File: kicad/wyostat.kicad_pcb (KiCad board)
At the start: 2 copper layers, 99.1 x 99.1 mm, 98 parts, among them J1 24 V AC IN, J10 Y2, J11 G, J12 W1, J13 USB_microAB, J14 W2, J16 5V_SEL, J2 OUT1, J3 OUT2, J4 OUT3, J5 I2C_ext1, J6 RH, J7 RC, J8 C, J9 Y1, Q1 BTA204S, Q2 BTA204S, Q3 BTA204S, U1 MOC3063M, U2 MOC3063M, U3 MOC3063M, U4 Wemos-Lolin, U5 MAX17502FATB+T, U6 DS3231N

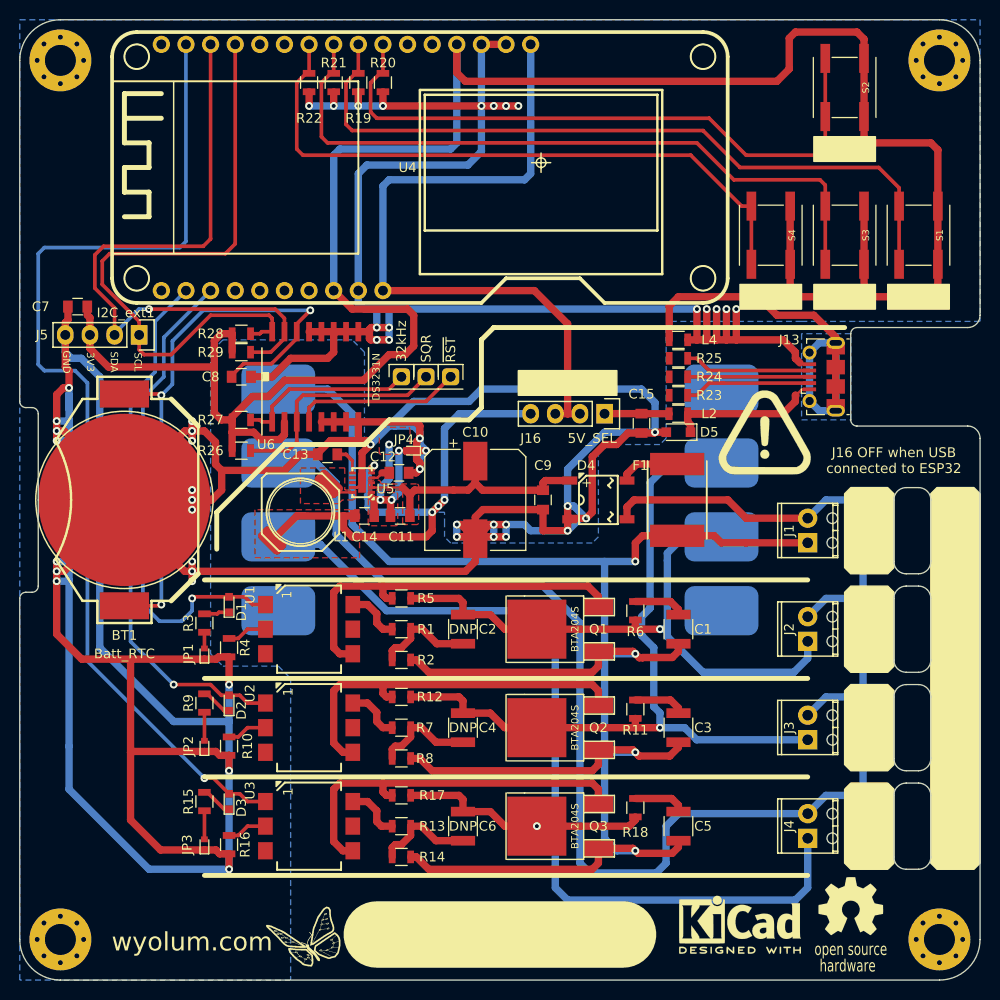
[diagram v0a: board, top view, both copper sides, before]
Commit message: footprint corrections on PCB
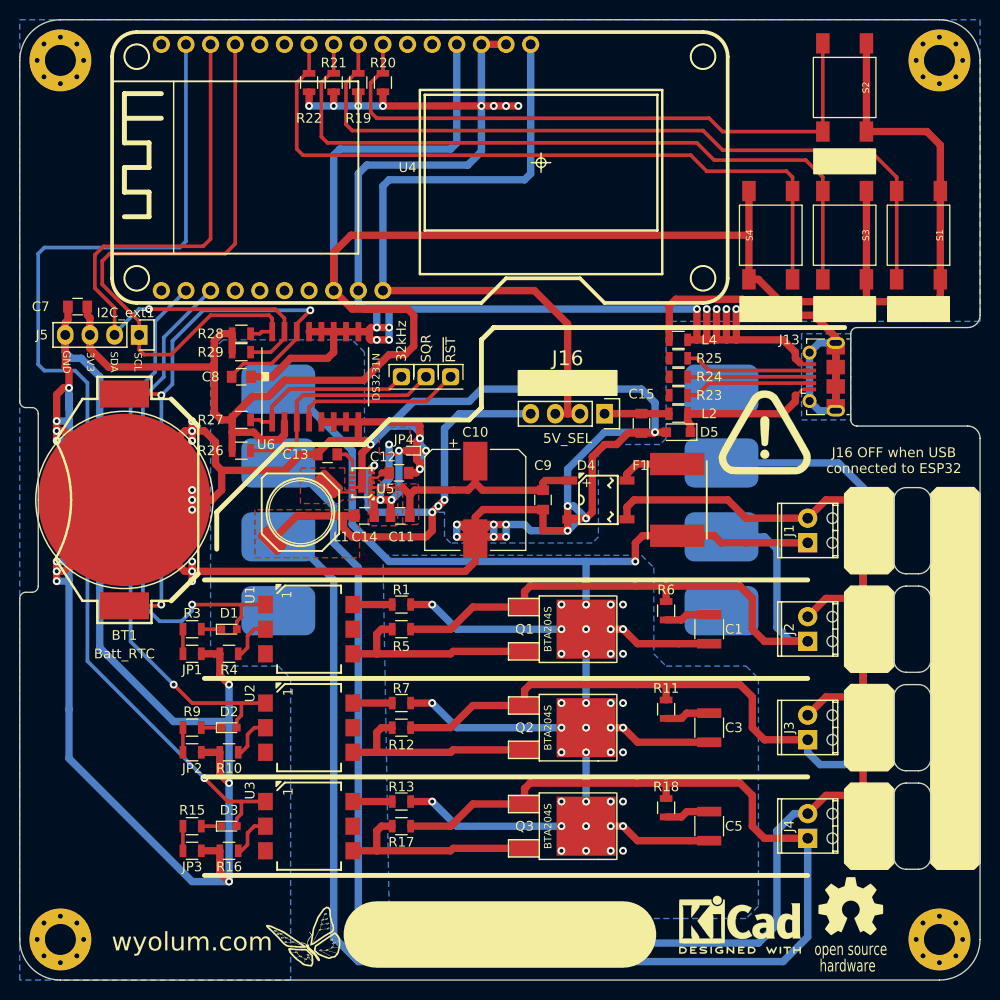
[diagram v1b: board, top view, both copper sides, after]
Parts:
- removed C2, C4, C6: 47nF,63V, wyostat_fp:C_1210
- removed R14, R2, R8: 0E, wyostat_fp:R_0805
- D5: footprint Diodes_SMD:D_SOD-323_HandSoldering -> wyostat_fp:D_SOD-323_HandSoldering
- JP1, JP2, JP3: footprint wyostat_fp:LED_0402 -> wyostat_fp:R_0805
- Logo5: renamed from G***; value LOGO -> logo_warning
- S1, S2, S3, S4: footprint wyostat_fp:SW_SPST_CK_KSCx -> wyostat_fp:SW_SPST_FSM6JSMA
- moved Q1 7.62 mm to (83.8, 94.6), turned to 270 degrees
- moved Q2 7.62 mm to (83.8, 104.8), turned to 270 degrees
- moved Q3 7.62 mm to (83.8, 114.9), turned to 270 degrees
- moved C1 3.18 mm to (102.9, 94.6)
- moved C3 3.18 mm to (102.9, 104.8)
- moved C5 3.18 mm to (102.9, 114.9)
- moved R12 3.18 mm to (71.1, 104.8)
- moved R11 3.17 mm to (98.4, 102.9), turned to 270 degrees
- moved R17 3.17 mm to (71.1, 114.9)
- moved R18 3.17 mm to (98.4, 113.0), turned to 270 degrees
- moved R5 3.17 mm to (71.1, 94.6)
- moved R6 3.17 mm to (98.4, 92.7), turned to 270 degrees
- moved R15 2.84 mm to (49.5, 114.9), turned to 0 degrees
- moved R9 2.84 mm to (49.5, 104.8), turned to 0 degrees
- moved D2 2.54 mm to (53.3, 104.8), turned to 0 degrees
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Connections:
- net /5V_IN1 renamed /5V_EXT
- net /5V_IN2 renamed /5V_USB
- J10 pad 1: /Y2 -> (no net)
- J14 pad 1: /W2 -> (no net)
- J7 pad 1: /Rc -> (no net)
- Q1 pad 1: /24Vac-H -> /OUT1
- Q1 pad 2: /OUT1 -> /24Vac-H
- Q2 pad 1: /24Vac-H -> /OUT2
- Q2 pad 2: /OUT2 -> /24Vac-H
- Q3 pad 1: /24Vac-H -> /OUT3
- Q3 pad 2: /OUT3 -> /24Vac-H
- R1 pad 1: Net-(C2-Pad1) -> /24Vac-H
- R13 pad 1: Net-(C6-Pad1) -> /24Vac-H
- R23 pad 1: /USB_D- -> (no net)
- R24 pad 1: /USB_D+ -> (no net)
- R25 pad 1: /USB_ID -> (no net)
- R7 pad 1: Net-(C4-Pad1) -> /24Vac-H
- U1 pad 3: Net-(U1-Pad3) -> (no net)
- U1 pad 5: Net-(U1-Pad5) -> (no net)
- U2 pad 3: Net-(U2-Pad3) -> (no net)
- U2 pad 5: Net-(U2-Pad5) -> (no net)
- U3 pad 3: Net-(U3-Pad3) -> (no net)
- U3 pad 5: Net-(U3-Pad5) -> (no net)
- U4 pad 1: Net-(U4-Pad1) -> (no net)
- U4 pad 11: Net-(U4-Pad11) -> (no net)
- U4 pad 12: Net-(U4-Pad12) -> (no net)
- U4 pad 20: Net-(U4-Pad20) -> (no net)
- U4 pad 21: Net-(U4-Pad21) -> (no net)
- U4 pad 22: Net-(U4-Pad22) -> (no net)
- U4 pad 23: Net-(U4-Pad23) -> (no net)
- U4 pad 26: Net-(U4-Pad26) -> (no net)
- U4 pad 5: Net-(U4-Pad5) -> (no net)
- U4 pad 6: Net-(U4-Pad6) -> (no net)
- U5 pad 7: Net-(U5-Pad7) -> (no net)
- U5 pad 8: /R -> (no net)
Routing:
- net GND: track 671.5 -> 620.7 mm
- net /OUT3: track 120.1 -> 156.1 mm, vias 1 -> 0
- net /OUT2: track 79.1 -> 100.2 mm, vias 1 -> 0
- net Net-(Q3-Pad3): track 39.1 -> 21.7 mm
- net Net-(Q2-Pad3): track 39.1 -> 21.7 mm
- net Net-(Q1-Pad3): track 39.1 -> 21.7 mm
- net /24Vac-C: track 170.8 -> 186.5 mm
- net Net-(C2-Pad1): track 10.4 -> 0.00 mm
- net Net-(C6-Pad1): track 10.4 -> 0.00 mm
- net Net-(C4-Pad1): track 10.4 -> 0.00 mm
- net /24Vac-H: track 203.3 -> 193.7 mm, vias 4 -> 40
- net /SW_M: track 66.8 -> 74.4 mm
- net /3V3: track 229.9 -> 235.9 mm
- net /OUT1: track 62.7 -> 67.6 mm, vias 1 -> 0
- net /IN3: track 106.4 -> 109.2 mm
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- added copper zone on B.Cu, net /24Vac-H

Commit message: PCB updated for 2nd round of prototype
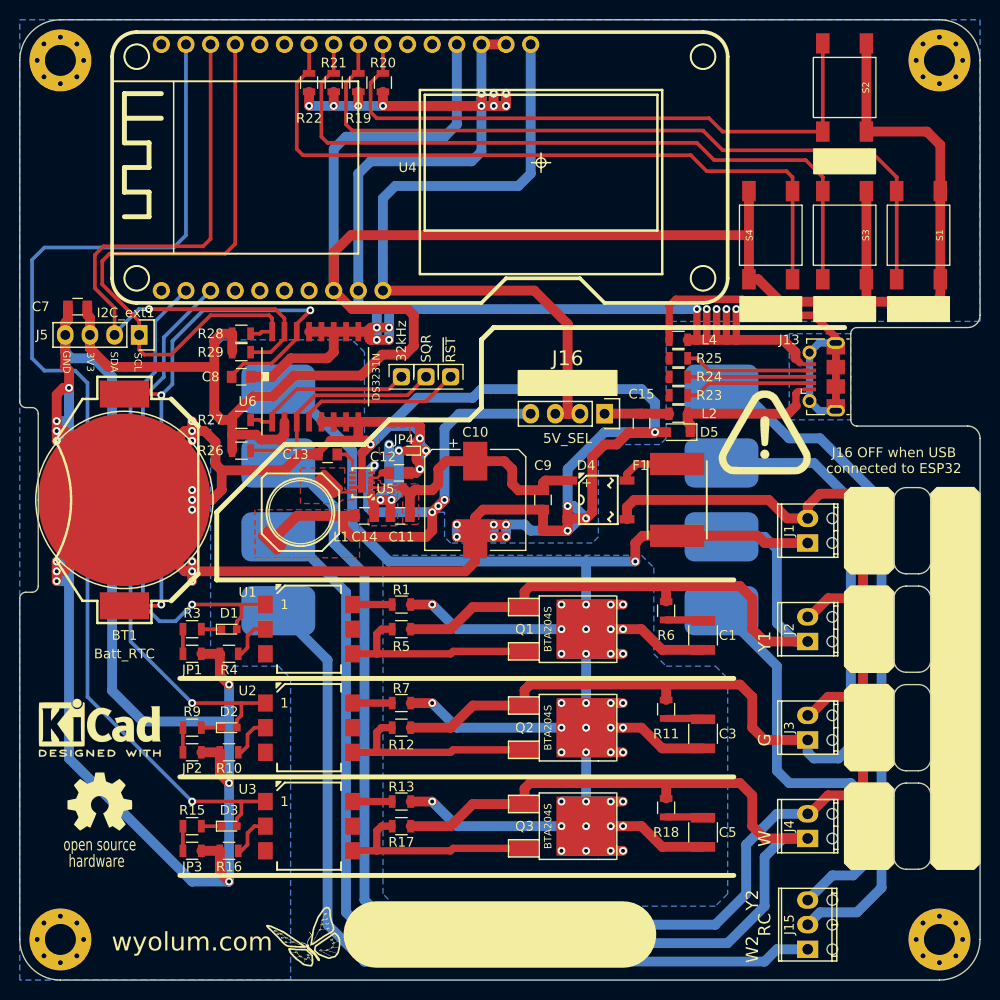
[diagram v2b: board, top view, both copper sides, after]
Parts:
- added J15: Conn_Spare, wyostat_fp:TerminalBlock_Pheonix_MPT-2.54mm_3pol, F.Cu at (113.0, 125.1)
- moved Logo2 78.2 mm to (40.0, 112.4)
- moved Logo3 69.1 mm to (40.0, 104.8)
- moved Logo4 26.7 mm to (81.9, 54.6)
- moved C1 0.90 mm to (102.2, 95.2)
- moved C3 0.90 mm to (102.2, 105.4)
- moved C5 0.90 mm to (102.2, 115.6)
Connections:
- J10 pad 1: (no net) -> /Y2
- J14 pad 1: (no net) -> /W2
- J7 pad 1: (no net) -> /RC
- R23 pad 1: (no net) -> /USB_D-
- R24 pad 1: (no net) -> /USB_D+
- R25 pad 1: (no net) -> /USB_ID
- U1 pad 3: (no net) -> Net-(U1-Pad3)
- U1 pad 5: (no net) -> Net-(U1-Pad5)
- U2 pad 3: (no net) -> Net-(U2-Pad3)
- U2 pad 5: (no net) -> Net-(U2-Pad5)
- U3 pad 3: (no net) -> Net-(U3-Pad3)
- U3 pad 5: (no net) -> Net-(U3-Pad5)
- U4 pad 1: (no net) -> Net-(U4-Pad1)
- U4 pad 11: (no net) -> Net-(U4-Pad11)
- U4 pad 12: (no net) -> Net-(U4-Pad12)
- U4 pad 20: (no net) -> Net-(U4-Pad20)
- U4 pad 21: (no net) -> Net-(U4-Pad21)
- U4 pad 22: (no net) -> Net-(U4-Pad22)
- U4 pad 23: (no net) -> Net-(U4-Pad23)
- U4 pad 26: (no net) -> Net-(U4-Pad26)
- U4 pad 5: (no net) -> Net-(U4-Pad5)
- U4 pad 6: (no net) -> Net-(U4-Pad6)
- U5 pad 7: (no net) -> Net-(U5-Pad7)
- U5 pad 8: (no net) -> /R
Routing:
- net /24Vac-H: track 193.7 -> 284.0 mm
- net /W2: track 0.00 -> 86.1 mm
- net /RC: track 0.00 -> 70.4 mm
- net /Y2: track 0.00 -> 43.2 mm
- net /OUT3: track 156.1 -> 148.3 mm
- net GND: track 620.7 -> 627.1 mm, vias 54 -> 56
- net /24Vac-C: track 186.5 -> 181.7 mm
- net /OUT2: track 100.2 -> 96.4 mm
- net /IN3: track 109.2 -> 111.5 mm
- net /40VDC: track 27.4 -> 28.8 mm
- net /USB+: track 17.5 -> 16.4 mm
- net /3V3: track 235.9 -> 235.1 mm
- net Net-(C5-Pad2): track 4.67 -> 3.85 mm
- net Net-(C1-Pad2): track 4.67 -> 3.85 mm
- net Net-(C3-Pad2): track 4.67 -> 3.85 mm
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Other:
- board text added: "W"
- board text added: "W2"

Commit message: added Sparkfun TMP102 footprint and PCB edges modified
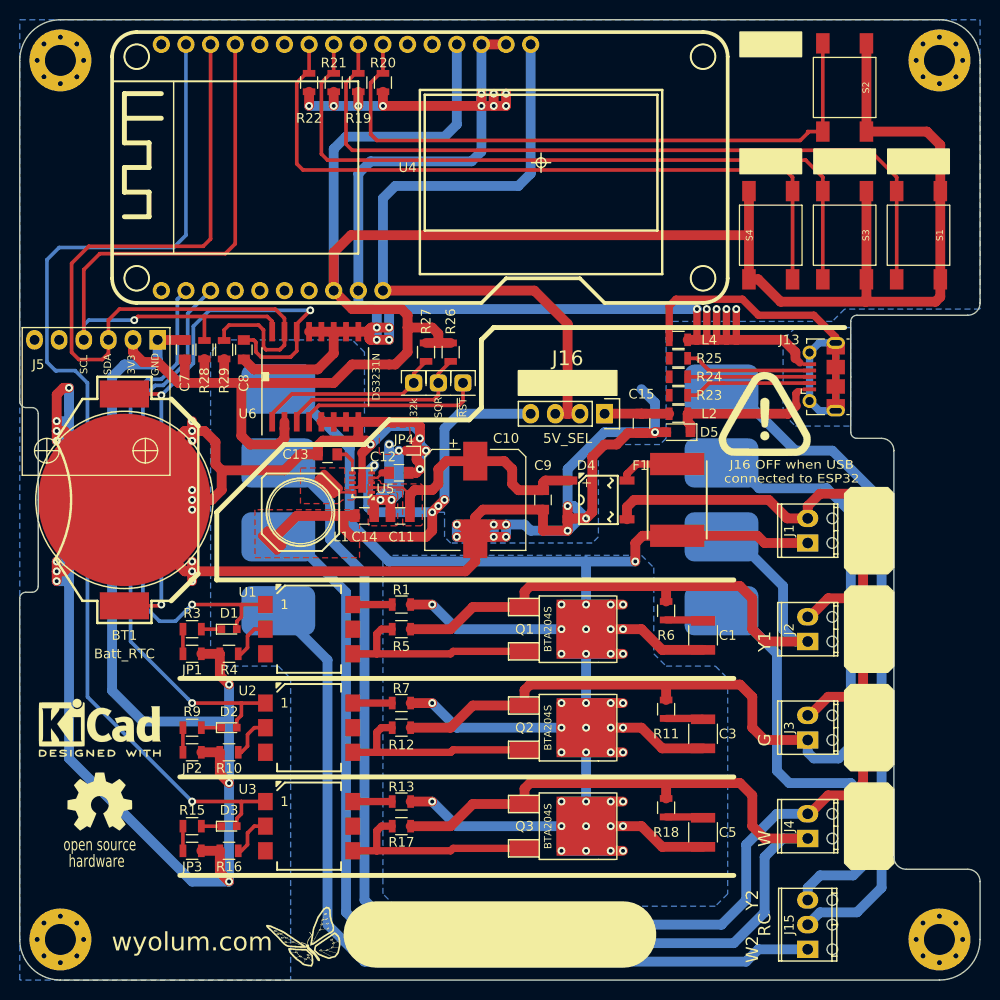
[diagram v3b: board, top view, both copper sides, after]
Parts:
- J5: footprint wyostat_fp:Pin_Header_Straight_1x04 -> wyostat_fp:Pin_Header_TMP102_1x06
- TP3: value 32kHz -> 32k
- moved R26 23.9 mm to (76.2, 66.0), turned to 270 degrees
- moved R27 20.3 mm to (73.7, 66.0), turned to 270 degrees
- moved C7 11.9 mm to (48.8, 65.8), turned to 90 degrees
- moved J5 5.74 mm to (46.0, 64.8)
- moved R28 4.15 mm to (50.8, 65.8), turned to 90 degrees
- moved C8 2.81 mm to (54.9, 65.8), turned to 270 degrees
- moved Logo5 1.91 mm to (108.6, 72.4)
- moved R29 1.80 mm to (52.8, 65.8), turned to 90 degrees
- moved TP2 1.42 mm to (74.9, 69.2)
- moved TP1 1.42 mm to (77.5, 69.2)
- moved TP3 1.42 mm to (72.4, 69.2)
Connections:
- J5 pad 1: /SCL -> GND
- J5 pad 2: /SDA -> /3V3
- J5 pad 3: /3V3 -> /SDA
- J5 pad 4: GND -> /SCL
- R23 pad 1: /USB_D- -> (no net)
- R24 pad 1: /USB_D+ -> (no net)
- R25 pad 1: /USB_ID -> (no net)
- U1 pad 3: Net-(U1-Pad3) -> (no net)
- U1 pad 5: Net-(U1-Pad5) -> (no net)
- U2 pad 3: Net-(U2-Pad3) -> (no net)
- U2 pad 5: Net-(U2-Pad5) -> (no net)
- U3 pad 3: Net-(U3-Pad3) -> (no net)
- U3 pad 5: Net-(U3-Pad5) -> (no net)
- U4 pad 1: Net-(U4-Pad1) -> (no net)
- U4 pad 11: Net-(U4-Pad11) -> (no net)
- U4 pad 12: Net-(U4-Pad12) -> (no net)
- U4 pad 20: Net-(U4-Pad20) -> (no net)
- U4 pad 21: Net-(U4-Pad21) -> (no net)
- U4 pad 22: Net-(U4-Pad22) -> (no net)
- U4 pad 23: Net-(U4-Pad23) -> (no net)
- U4 pad 26: Net-(U4-Pad26) -> (no net)
- U4 pad 5: Net-(U4-Pad5) -> (no net)
- U4 pad 6: Net-(U4-Pad6) -> (no net)
- U5 pad 7: Net-(U5-Pad7) -> (no net)
- U5 pad 8: /R -> (no net)
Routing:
- net GND: track 627.1 -> 595.1 mm
- net /SDA: track 67.1 -> 84.0 mm, vias 1 -> 0
- net /3V3: track 235.1 -> 229.9 mm
- net /SCL: track 65.2 -> 69.6 mm, vias 0 -> 1
- net /IN3: track 111.5 -> 108.6 mm
- net /rtc_ds3231/SQR: track 23.0 -> 20.2 mm
- net /SW_I: track 64.3 -> 66.4 mm
- net /rtc_ds3231/RESET: track 17.0 -> 19.1 mm
- net /OUT1: track 67.4 -> 65.5 mm
- net /Y2: track 43.2 -> 44.7 mm
- net /rtc_ds3231/32kHz: track 18.1 -> 19.5 mm
- net /SW_E: track 78.5 -> 79.7 mm
- net /SW_D: track 74.2 -> 75.3 mm
- net /SW_M: track 74.4 -> 75.3 mm
- net /IN2: track 57.8 -> 58.7 mm
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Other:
- outline, holes or cut-outs redrawn
